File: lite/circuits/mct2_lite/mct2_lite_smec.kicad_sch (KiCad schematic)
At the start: 0 parts

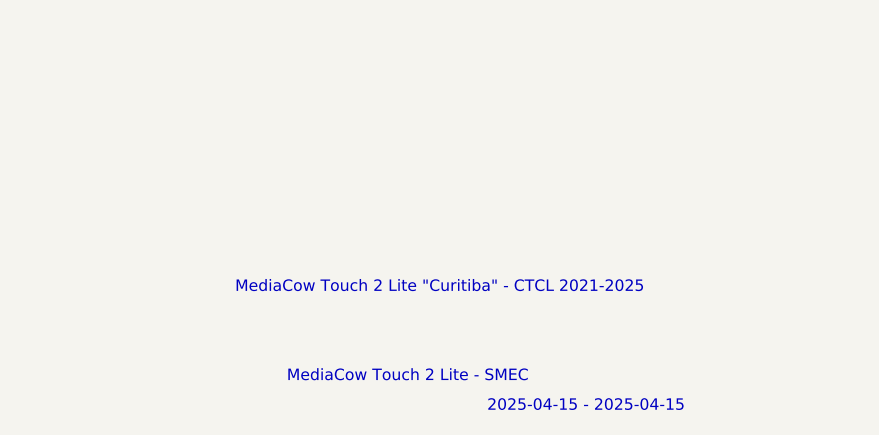
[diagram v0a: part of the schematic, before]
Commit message: 20250426-1 Remove current codename
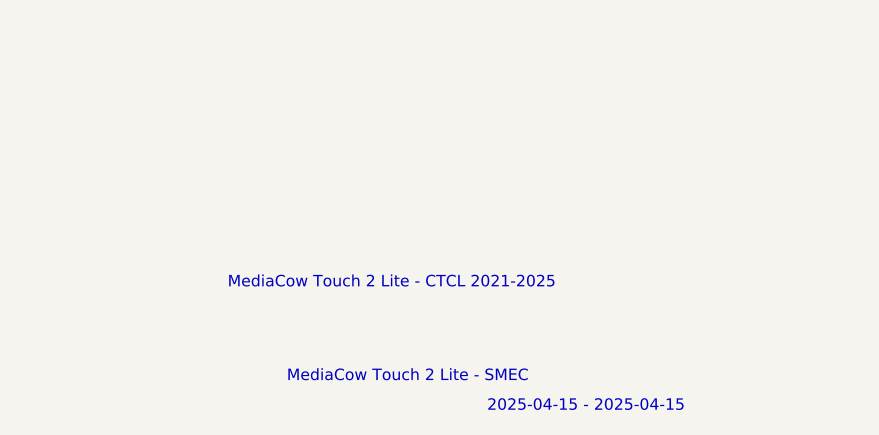
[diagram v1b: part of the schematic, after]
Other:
- note added: "MediaCow Touch 2 Lite - CTCL 2021-2025"
- note removed: "MediaCow Touch 2 Lite "Curitiba" - CTCL 2021-2025"
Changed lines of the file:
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@@
 		)
 	)
-	(text "MediaCow Touch 2 Lite \"Curitiba\" - CTCL 2021-2025"
+	(text "MediaCow Touch 2 Lite - CTCL 2021-2025"
 		(exclude_from_sim no)
-		(at 204.724 180.086 0)
+		(at 199.39 179.578 0)
 		(effects
 			(font

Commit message: 20250504-1
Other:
- note added: "2025-04-15 - 2025-04-29"
- note added: "MediaCow Touch 2 Lite "Curitiba" - CTCL 2021-2025"
- note removed: "2025-04-15 - 2025-04-15"
- note removed: "MediaCow Touch 2 Lite - CTCL 2021-2025"
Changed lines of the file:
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@@
 		)
 	)
-	(text "MediaCow Touch 2 Lite - CTCL 2021-2025"
+	(text "MediaCow Touch 2 Lite \"Curitiba\" - CTCL 2021-2025"
 		(exclude_from_sim no)
-		(at 199.39 179.578 0)
+		(at 204.47 180.086 0)
 		(effects
 			(font
@@
 		)
 	)
-	(text "2025-04-15 - 2025-04-15"
+	(text "2025-04-15 - 2025-04-29"
 		(exclude_from_sim no)
 		(at 220.98 193.294 0)

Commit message: 20250509-1
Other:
- note removed: "2025-04-15 - 2025-04-29"
- note removed: "MediaCow Touch 2 Lite "Curitiba" - CTCL 2021-2025"
- note removed: "MediaCow Touch 2 Lite - SMEC"
- company: (none) -> CTCL 2021-2025
- title: (none) -> MediaCow Touch 2 "Curitiba" - SMEC
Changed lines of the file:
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@@
 	(generator_version "8.0")
 	(paper "A4")
-	(text "MediaCow Touch 2 Lite - SMEC"
-		(exclude_from_sim no)
-		(at 201.168 189.992 0)
-		(effects
-			(font
-				(size 1.27 1.27)
-			)
-		)
-	)
-	(text "MediaCow Touch 2 Lite \"Curitiba\" - CTCL 2021-2025"
-		(exclude_from_sim no)
-		(at 204.47 180.086 0)
-		(effects
-			(font
-				(size 1.27 1.27)
-			)
-		)
-	)
-	(text "2025-04-15 - 2025-04-29"
-		(exclude_from_sim no)
-		(at 220.98 193.294 0)
-		(effects
-			(font
-				(size 1.27 1.27)
-			)
-		)
+	(title_block
+		(title "MediaCow Touch 2 \"Curitiba\" - SMEC")
+		(date "2025-03-23 - 2025-05-09")
+		(company "CTCL 2021-2025")
 	)
 	(global_label "SOM_PWRBTN"

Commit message: 20250524-1
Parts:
- added U?: STM32L071V8Tx, Package_QFP:LQFP-100_14x14mm_P0.5mm, symbol MCU_ST_STM32L0:STM32L071V8Tx
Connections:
- new net: U?.27 (VSS), U?.49 (VSS), U?.74 (VSS), U?.99 (VSS)

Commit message: 20250529-1
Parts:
- gave numbers to parts that had none: 1
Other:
- moved on the sheet: U28
